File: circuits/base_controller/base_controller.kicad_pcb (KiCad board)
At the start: 2 copper layers, 95 x 95 mm, 45 parts, among them J1 OUTPUT, J2 INPUT, J3 3V3, J4 5V, J5 USB_B_Micro, J6 Barrel_Jack, Q1 S8050, U1 ESP32-WROOM-32, U2 CP2102N-A01-GQFN24, U3 AMS1117-5.0

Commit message: Small edit
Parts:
- R5, R8: moved to B.Cu
- moved J4 141.6 mm to (106.7, 132.6), turned to 270 degrees
- moved J3 126.3 mm to (106.4, 117.9), turned to 270 degrees
- moved J5 125.2 mm to (156.7, 147.4)
- moved D1 119.0 mm to (155.2, 137.9)
- moved R5 112.2 mm to (155.4, 116.8), turned to 270 degrees
- moved Q1 109.2 mm to (139.2, 102.9), turned to 90 degrees
- moved R8 12.8 mm to (163.1, 138.2), turned to 180 degrees
- turned R3 to 270 degrees
- turned R7 to 270 degrees
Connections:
- J5 pad 1: Net-(D1-Pad4) -> Net-(D1-Pad2)
- J5 pad 2: Net-(D1-Pad2) -> Net-(D1-Pad3)
- J5 pad 3: Net-(D1-Pad3) -> Net-(D1-Pad4)
- R4 pad 1: Net-(D1-Pad4) -> Net-(D1-Pad2)
- U2 pad 3: Net-(D1-Pad3) -> Net-(D1-Pad4)
- U2 pad 4: Net-(D1-Pad2) -> Net-(D1-Pad3)
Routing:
- net Earth: track 42.9 -> 100.5 mm, vias 0 -> 2
- net Net-(D1-Pad2): track 0.00 -> 34.1 mm, vias 0 -> 1
- net Net-(D1-Pad4): track 0.00 -> 22.7 mm, vias 0 -> 1
- net Net-(D1-Pad3): track 0.00 -> 21.9 mm, vias 0 -> 1
- net Net-(R7-Pad2): track 0.00 -> 20.3 mm
- net Net-(R4-Pad2): track 0.00 -> 18.2 mm
- net Net-(R6-Pad2): track 0.00 -> 17.2 mm
- net Net-(R3-Pad2): track 0.00 -> 10.9 mm
- net Net-(R8-Pad2): track 0.00 -> 5.68 mm
- net +3V3: track 42.9 -> 44.4 mm
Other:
- board text added: "+"
- board text added: "-"

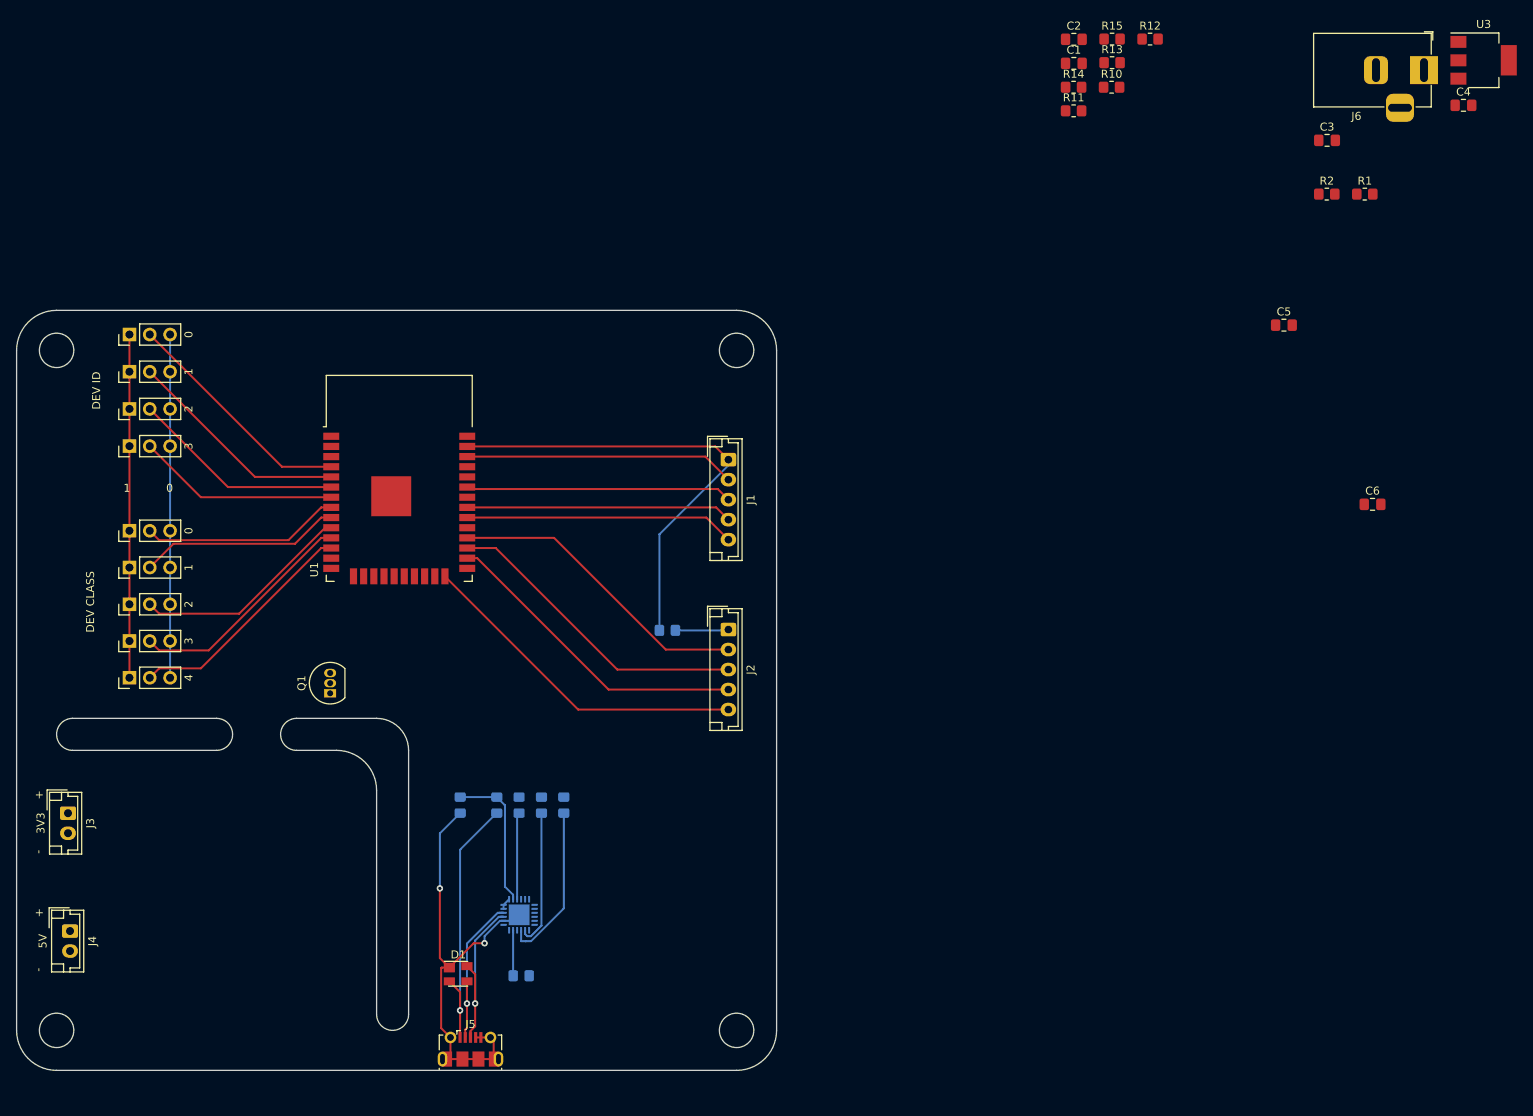
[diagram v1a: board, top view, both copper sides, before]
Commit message: Made break-out boards for the motors
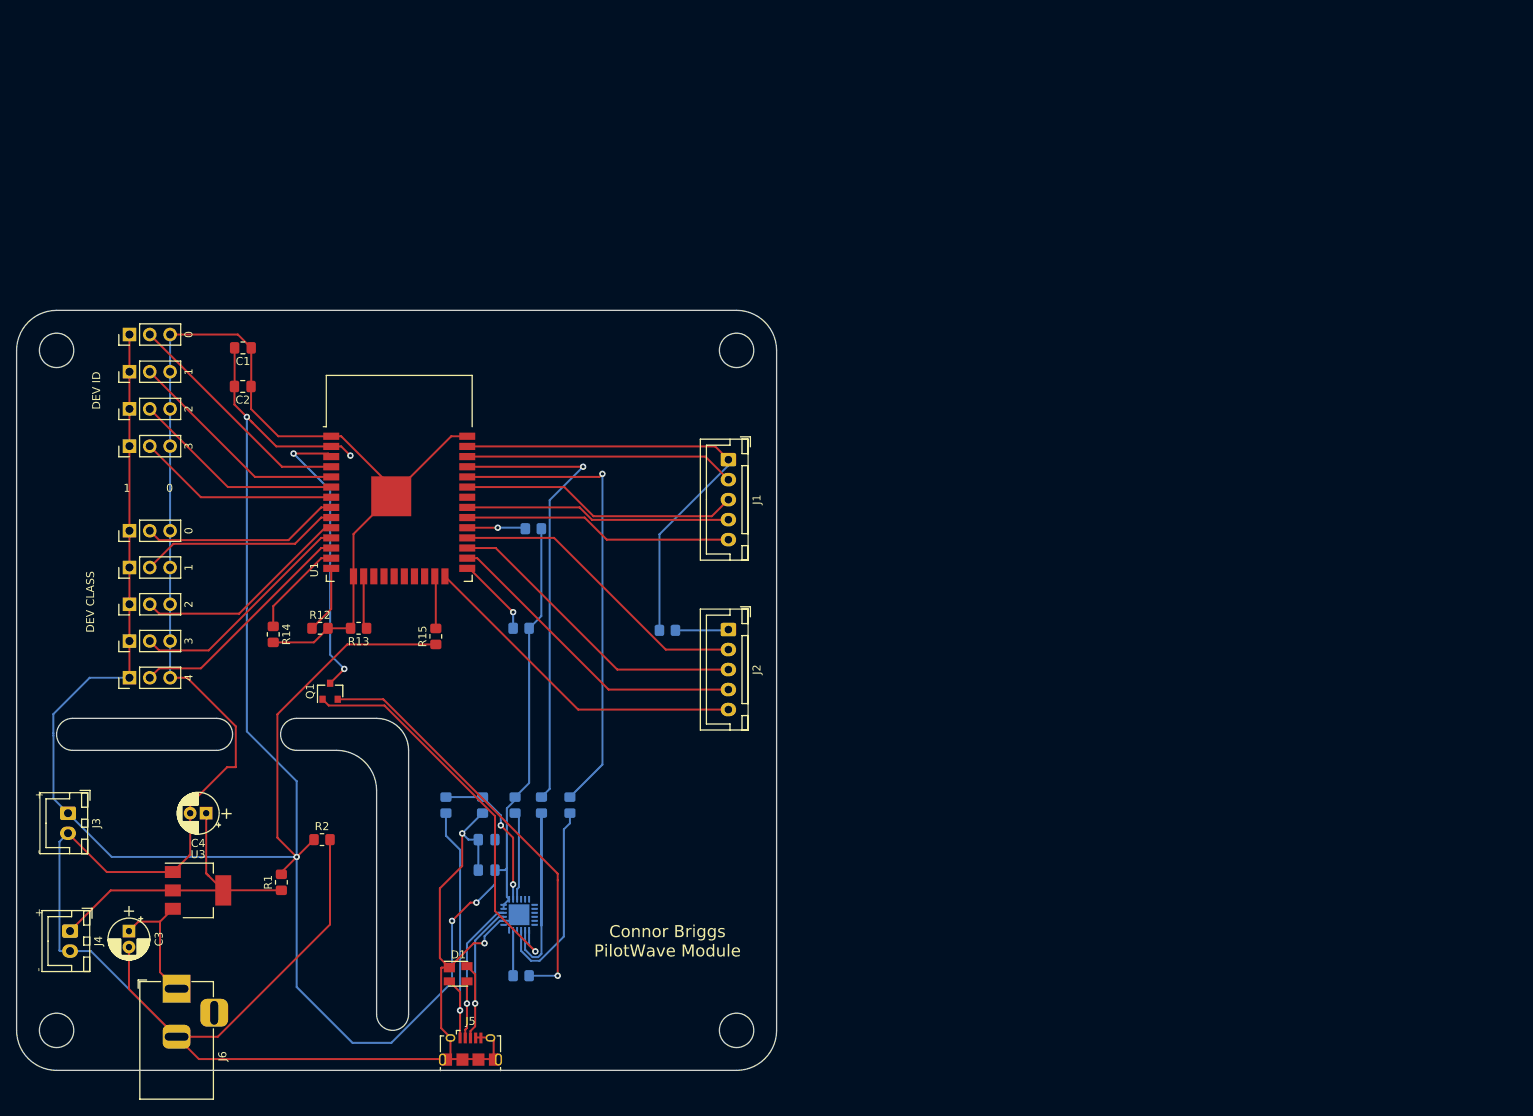
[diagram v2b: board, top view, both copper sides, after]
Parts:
- C3, C4: footprint Capacitor_SMD:C_0805_2012Metric_Pad1.18x1.45mm_HandSolder -> Capacitor_THT:CP_Radial_D5.0mm_P2.00mm
- C5, C6, R10, R11: moved to B.Cu
- J1, J2: footprint Connector_JST:JST_EH_B5B-EH-A_1x05_P2.50mm_Vertical -> Connector_JST:JST_XH_B5B-XH-A_1x05_P2.50mm_Vertical
- J3, J4: footprint Connector_JST:JST_EH_B2B-EH-A_1x02_P2.50mm_Vertical -> Connector_JST:JST_XH_B2B-XH-A_1x02_P2.50mm_Vertical
- J5: footprint Connector_USB:USB_Micro-B_Molex-105017-0001 -> Connector_USB:USB_Micro-B_Amphenol_10118194_Horizontal
- Q1: footprint Package_TO_SOT_THT:TO-92_Inline -> Package_TO_SOT_SMD:SOT-23
- moved J6 193.6 mm to (120.0, 139.8), turned to 90 degrees
- moved U3 191.3 mm to (122.7, 127.5)
- moved C4 180.4 mm to (123.7, 117.9), turned to 180 degrees
- moved C3 179.4 mm to (114.0, 132.6), turned to 270 degrees
- moved R1 160.4 mm to (133.1, 126.5), turned to 90 degrees
- moved R2 149.3 mm to (138.2, 121.2)
- moved R12 127.2 mm to (137.9, 94.7)
- moved R14 121.2 mm to (132.1, 95.5), turned to 270 degrees
- moved C5 120.7 mm to (158.8, 125.0), turned to 180 degrees
- moved C6 118.4 mm to (158.8, 121.2), turned to 180 degrees
- moved R13 117.8 mm to (142.7, 94.7), turned to 180 degrees
- moved R15 112.8 mm to (152.4, 95.8), turned to 90 degrees
- moved C2 112.6 mm to (128.3, 64.5), turned to 180 degrees
- moved C1 109.8 mm to (128.3, 59.7), turned to 180 degrees
- moved R10 100.1 mm to (163.1, 94.7), turned to 180 degrees
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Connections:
- R4 pad 1: Net-(D1-Pad2) -> Net-(R4-Pad1)
- R4 pad 2: Net-(R4-Pad2) -> Net-(D1-Pad2)
- R5 pad 1: Net-(R4-Pad2) -> Net-(R4-Pad1)
- U2 pad 8: Net-(R4-Pad2) -> Net-(R4-Pad1)
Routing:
- net +3V3: track 44.4 -> 342.2 mm, vias 0 -> 5
- net Earth: track 100.5 -> 357.2 mm
- net RXD0: track 0.00 -> 59.1 mm, vias 0 -> 1
- net TXD0: track 0.00 -> 57.9 mm, vias 0 -> 1
- net Net-(Q1-Pad2): track 0.00 -> 52.9 mm, vias 0 -> 1
- net Net-(Q1-Pad1): track 0.00 -> 49.6 mm, vias 0 -> 1
- net +5V: track 0.00 -> 39.5 mm
- net EN: track 0.00 -> 37.2 mm, vias 0 -> 2
- net Net-(R6-Pad2): track 17.2 -> 36.7 mm
- net Net-(R4-Pad1): track 0.00 -> 18.9 mm, vias 0 -> 2
- net Net-(R4-Pad2): track 18.2 -> 0.00 mm
- net Net-(C3-Pad1): track 0.00 -> 15.9 mm
- net MTMS: track 0.00 -> 12.3 mm
- net IO0: track 0.00 -> 10.0 mm, vias 0 -> 1
- net MTDI: track 0.00 -> 8.49 mm
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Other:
- board text added: "Connor Briggs PilotWave Module"

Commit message: Big changes
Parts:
- U3: footprint Package_TO_SOT_SMD:SOT-223-3_TabPin2 -> Package_TO_SOT_SMD:TO-252-3_TabPin4
- moved U3 1.35 mm to (124.0, 127.5)
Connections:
- U1 pad 17: Net-(U1-Pad17) -> unconnected-(U1-Pad17)
- U1 pad 18: Net-(U1-Pad18) -> unconnected-(U1-Pad18)
- U1 pad 19: Net-(U1-Pad19) -> unconnected-(U1-Pad19)
- U1 pad 20: Net-(U1-Pad20) -> unconnected-(U1-Pad20)
- U1 pad 21: Net-(U1-Pad21) -> unconnected-(U1-Pad21)
- U1 pad 22: Net-(U1-Pad22) -> unconnected-(U1-Pad22)
- U1 pad 32: Net-(U1-Pad32) -> unconnected-(U1-Pad32)
- U2 pad 1: Net-(U2-Pad1) -> unconnected-(U2-Pad1)
- U2 pad 10: Net-(U2-Pad10) -> unconnected-(U2-Pad10)
- U2 pad 11: Net-(U2-Pad11) -> unconnected-(U2-Pad11)
- U2 pad 12: Net-(U2-Pad12) -> unconnected-(U2-Pad12)
- U2 pad 13: Net-(U2-Pad13) -> unconnected-(U2-Pad13)
- U2 pad 14: Net-(U2-Pad14) -> unconnected-(U2-Pad14)
- U2 pad 15: Net-(U2-Pad15) -> unconnected-(U2-Pad15)
- U2 pad 16: Net-(U2-Pad16) -> unconnected-(U2-Pad16)
- U2 pad 17: Net-(U2-Pad17) -> unconnected-(U2-Pad17)
- U2 pad 18: Net-(U2-Pad18) -> unconnected-(U2-Pad18)
- U2 pad 22: Net-(U2-Pad22) -> unconnected-(U2-Pad22)
- U2 pad 24: Net-(U2-Pad24) -> unconnected-(U2-Pad24)
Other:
- net class Default removed

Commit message: Big updates
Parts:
- removed C3: 10 uF, Capacitor_THT:CP_Radial_D5.0mm_P2.00mm
- removed C4: 22 uF, Capacitor_THT:CP_Radial_D5.0mm_P2.00mm
- removed C5: 4.7 uF, Capacitor_SMD:C_0805_2012Metric_Pad1.18x1.45mm_HandSolder
- removed C6: 0.1 uF, Capacitor_SMD:C_0805_2012Metric_Pad1.18x1.45mm_HandSolder
- removed JP1, JP6: 0, Connector_PinHeader_2.54mm:PinHeader_1x03_P2.54mm_Vertical
- removed JP2, JP7: 1, Connector_PinHeader_2.54mm:PinHeader_1x03_P2.54mm_Vertical
- removed JP3, JP8: 2, Connector_PinHeader_2.54mm:PinHeader_1x03_P2.54mm_Vertical
- removed JP4, JP9: 3, Connector_PinHeader_2.54mm:PinHeader_1x03_P2.54mm_Vertical
- removed JP5: 4, Connector_PinHeader_2.54mm:PinHeader_1x03_P2.54mm_Vertical
- removed Q1: S8050, Package_TO_SOT_SMD:SOT-23
- removed R10, R11, R12, R13, R14, R15: 10 K, Resistor_SMD:R_0805_2012Metric_Pad1.20x1.40mm_HandSolder
- removed R9: 1 K, Resistor_SMD:R_0805_2012Metric_Pad1.20x1.40mm_HandSolder
- removed the REF** at (105.0, 145.0)
- removed the REF** at (105.0, 60.0)
- removed the REF** at (190.0, 60.0)
- removed the REF** at (190.0, 145.0)
- removed U2: CP2102N-A01-GQFN24, Package_DFN_QFN:QFN-24-1EP_4x4mm_P0.5mm_EP2.6x2.6mm
- removed U3: AMS1117-5.0, Package_TO_SOT_SMD:TO-252-3_TabPin4
- added D2: DIODE, Diode_SMD:D_0805_2012Metric_Pad1.15x1.40mm_HandSolder, F.Cu at (109.2, 80.1)
- added D3: DIODE, Diode_SMD:D_0805_2012Metric_Pad1.15x1.40mm_HandSolder, F.Cu at (109.2, 84.3)
- added D4: DIODE, Diode_SMD:D_0805_2012Metric_Pad1.15x1.40mm_HandSolder, F.Cu at (109.2, 88.4)
- added D5: DIODE, Diode_SMD:D_0805_2012Metric_Pad1.15x1.40mm_HandSolder, F.Cu at (109.2, 92.5)
- added REF**: MountingHole_3.2mm_M3_Pad, MountingHole:MountingHole_3.2mm_M3_Pad, F.Cu at (190.0, 60.0)
- added REF**: MountingHole_3.2mm_M3_Pad, MountingHole:MountingHole_3.2mm_M3_Pad, F.Cu at (105.0, 60.0)
- added REF**: MountingHole_3.2mm_M3_Pad, MountingHole:MountingHole_3.2mm_M3_Pad, F.Cu at (190.0, 115.0)
- added REF**: MountingHole_3.2mm_M3_Pad, MountingHole:MountingHole_3.2mm_M3_Pad, F.Cu at (105.0, 115.0)
- added SW1: DEV_CLASS, Button_Switch_THT:SW_DIP_SPSTx05_Slide_9.78x14.88mm_W7.62mm_P2.54mm, F.Cu at (115.1, 78.2)
- D1: value SP0503BAHT -> DIODE; footprint Package_TO_SOT_SMD:SOT-143 -> Diode_SMD:D_0805_2012Metric_Pad1.15x1.40mm_HandSolder
- J1: value OUTPUT -> JTAG; footprint Connector_JST:JST_XH_B5B-XH-A_1x05_P2.50mm_Vertical -> Connector_PinHeader_2.54mm:PinHeader_2x05_P2.54mm_Vertical
- J2: value INPUT -> OUTPUT
- J3: value 3V3 -> INPUT; footprint Connector_JST:JST_XH_B2B-XH-A_1x02_P2.50mm_Vertical -> Connector_JST:JST_XH_B5B-XH-A_1x05_P2.50mm_Vertical
- J4: value 5V -> 3V3
- J5: value USB_B_Micro -> 5V; footprint Connector_USB:USB_Micro-B_Amphenol_10118194_Horizontal -> Connector_JST:JST_XH_B2B-XH-A_1x02_P2.50mm_Vertical
- J6: value Barrel_Jack -> POWER_IN; footprint Connector_BarrelJack:BarrelJack_Horizontal -> Connector_JST:JST_XH_B4B-XH-A_1x04_P2.50mm_Vertical; moved to B.Cu
- R1: value 1 K -> 10 K; moved to B.Cu
- R2: value 2 K -> 10 K; moved to B.Cu
- R3: moved to F.Cu
- R4: value 22.1 K -> 4.7 k
- R5: value 47.5 K -> 4.7 k
- R6, R7: value 1 K -> 4.7 k
- R8: value 10 K -> 4.7 k
- moved D1 77.2 mm to (109.2, 75.9), turned to 180 degrees
- moved J3 70.9 mm to (175.0, 100.0)
- moved R8 59.1 mm to (129.5, 89.5), turned to 0 degrees
- moved R7 55.8 mm to (129.5, 77.5), turned to 180 degrees
- moved J4 53.3 mm to (155.0, 110.0)
- moved R1 51.5 mm to (166.4, 87.1), turned to -90 degrees
- moved R2 47.8 mm to (166.4, 82.6), turned to -90 degrees
- moved J1 47.0 mm to (150.0, 100.0), turned to 90 degrees
- moved R5 45.5 mm to (129.5, 81.5), turned to 180 degrees
- moved R6 43.0 mm to (129.5, 93.5), turned to 0 degrees
- moved R4 39.5 mm to (129.5, 85.5), turned to 180 degrees
- moved J5 39.2 mm to (145.0, 110.0), turned to -90 degrees
- moved J6 31.4 mm to (130.0, 110.0)
- moved R3 31.2 mm to (182.1, 92.7)
- moved J2 24.3 mm to (175.0, 75.0)
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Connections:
- C1 pad 2: +3V3 -> EN
- C2 pad 2: +3V3 -> EN
- D1 pad 1: Earth -> Net-(D1-Pad1)
- D1 pad 2: Net-(D1-Pad2) -> Earth
- J1 pad 1: DATA_IO -> EN
- J1 pad 2: SHCP_1 -> MTMS
- J1 pad 3: STCP_1 -> Earth
- J1 pad 4: OE_1 -> MTCK
- J1 pad 5: MR_1 -> Earth
- J2 pad 1: Net-(J2-Pad1) -> DATA_IO
- J2 pad 2: SHCP_2 -> SHCP_1
- J2 pad 3: STCP_2 -> STCP_1
- J2 pad 4: PL_2 -> OE_1
- J2 pad 5: MR_2 -> MR_1
- J3 pad 1: +3V3 -> Net-(J3-Pad1)
- J3 pad 2: Earth -> SHCP_2
- J4 pad 1: +5V -> EN
- J5 pad 1: Net-(D1-Pad2) -> +5V
- J5 pad 2: Net-(D1-Pad3) -> Earth
- J6 pad 1: Net-(C3-Pad1) -> Earth
- J6 pad 2: Earth -> +5V
- J6 pad 3: (no net) -> EN
- R1 pad 1: +5V -> EN
- R1 pad 2: +3V3 -> IO0
- R2 pad 1: +3V3 -> EN
- R2 pad 2: Earth -> IO5
- R3 pad 1: +3V3 -> DATA_IO
- R3 pad 2: Net-(R3-Pad2) -> Net-(J3-Pad1)
- R4 pad 1: Net-(R4-Pad1) -> EN
- R4 pad 2: Net-(D1-Pad2) -> DEVCL_2
- R5 pad 1: Net-(R4-Pad1) -> EN
- R5 pad 2: Earth -> DEVCL_1
- R6 pad 1: TXD0 -> DEVCL_4
- R6 pad 2: Net-(R6-Pad2) -> EN
- R7 pad 1: RXD0 -> EN
- R7 pad 2: Net-(R7-Pad2) -> DEVCL_0
- R8 pad 1: Net-(Q1-Pad2) -> DEVCL_3
- R8 pad 2: Net-(R8-Pad2) -> EN
- U1 pad 2: +3V3 -> EN
- U1 pad 34: RXD0 -> unconnected-(U1-Pad34)
- U1 pad 35: TXD0 -> unconnected-(U1-Pad35)
- U1 pad 4: DEVID_0 -> unconnected-(U1-Pad4)
- U1 pad 5: DEVID_1 -> unconnected-(U1-Pad5)
- U1 pad 6: DEVID_2 -> unconnected-(U1-Pad6)
- U1 pad 7: DEVID_3 -> unconnected-(U1-Pad7)
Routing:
- net +3V3: track 342.2 -> 0.00 mm, vias 5 -> 0
- net Earth: track 357.2 -> 167.9 mm, vias 2 -> 0
- net EN: track 37.2 -> 110.2 mm, vias 2 -> 1
- net RXD0: track 59.1 -> 0.00 mm, vias 1 -> 0
- net TXD0: track 57.9 -> 0.00 mm, vias 1 -> 0
- net Net-(Q1-Pad2): track 52.9 -> 0.00 mm, vias 1 -> 0
- net Net-(Q1-Pad1): track 49.6 -> 0.00 mm, vias 1 -> 0
- net Net-(R6-Pad2): track 36.7 -> 0.00 mm
- net Net-(D1-Pad2): track 33.0 -> 0.00 mm, vias 1 -> 0
- net DEVID_0: track 29.5 -> 0.00 mm
- net DEVID_1: track 28.1 -> 0.00 mm
- net DEVID_2: track 26.7 -> 0.00 mm
- net Net-(R7-Pad2): track 25.4 -> 0.00 mm
- net DEVID_3: track 25.3 -> 0.00 mm
- net +5V: track 39.5 -> 16.0 mm
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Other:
- board size 95 x 95 mm -> 95 x 65 mm
- board text removed: "+"
- board text removed: "-"
- board text removed: "0"
- board text removed: "1"
- board text removed: "DEV CLASS"
- board text removed: "DEV ID"
